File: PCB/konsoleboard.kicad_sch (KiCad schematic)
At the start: 0 parts

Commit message: Finished making the schematic, imma work on the PCB next
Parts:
- added A1: RaspberryPi_Pico, Module:RaspberryPi_Pico_Common_THT, symbol MCU_Module:RaspberryPi_Pico
- added BZ1: Buzzer, Buzzer_Beeper:Buzzer_Mallory_AST1109MLTRQ, symbol Device:Buzzer
- added SW1, SW10, SW2, SW3, SW4, SW5, SW6, SW7, SW8: SW_Push, Button_Switch_THT:SW_PUSH-12mm, symbol Switch:SW_Push
- added SW9: SW_Wuerth_450301014042, Button_Switch_THT:SW_Slide-03_Wuerth-WS-SLTV_10x2.5x6.4_P2.54mm, symbol Switch:SW_Wuerth_450301014042
- added U1: DM-OLED096-636, DM-OLED096-636:MODULE_DM-OLED096-636, symbol DM-OLED096-636:DM-OLED096-636
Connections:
- new net +3V3: A1.36 (3V3), SW9.1 (B), U1.2 (VCC_IN)
- new net BuzzerP: A1.16 (GPIO12), BZ1.1 (+)
- new net GND: A1.13 (GND), A1.18 (GND), A1.23 (GND), A1.28 (GND), A1.3 (GND), A1.38 (GND), A1.8 (GND), BZ1.2 (-), SW1.1, SW10.1, SW2.1, SW3.1, SW4.1, SW5.1, SW6.1, SW7.1, SW8.1, U1.1 (GND)
- new net LP1: A1.2 (GPIO1), SW1.2
- new net LP2: A1.4 (GPIO2), SW2.2
- new net LP3: A1.5 (GPIO3), SW3.2
- new net LP4: A1.6 (GPIO4), SW4.2
- new net RP1: A1.7 (GPIO5), SW5.2
- new net RP2: A1.9 (GPIO6), SW6.2
- new net RP3: A1.10 (GPIO7), SW7.2
- new net RP4: A1.11 (GPIO8), SW8.2
- new net RP5: A1.12 (GPIO9), SW10.2
- new net SCL: A1.15 (GPIO11), U1.3 (SCL)
- new net SDA: A1.14 (GPIO10), U1.4 (SDA)
- new net ToggleSwitch: A1.37 (3V3_EN), SW9.2 (C)
- no-connect marks 0 -> 20

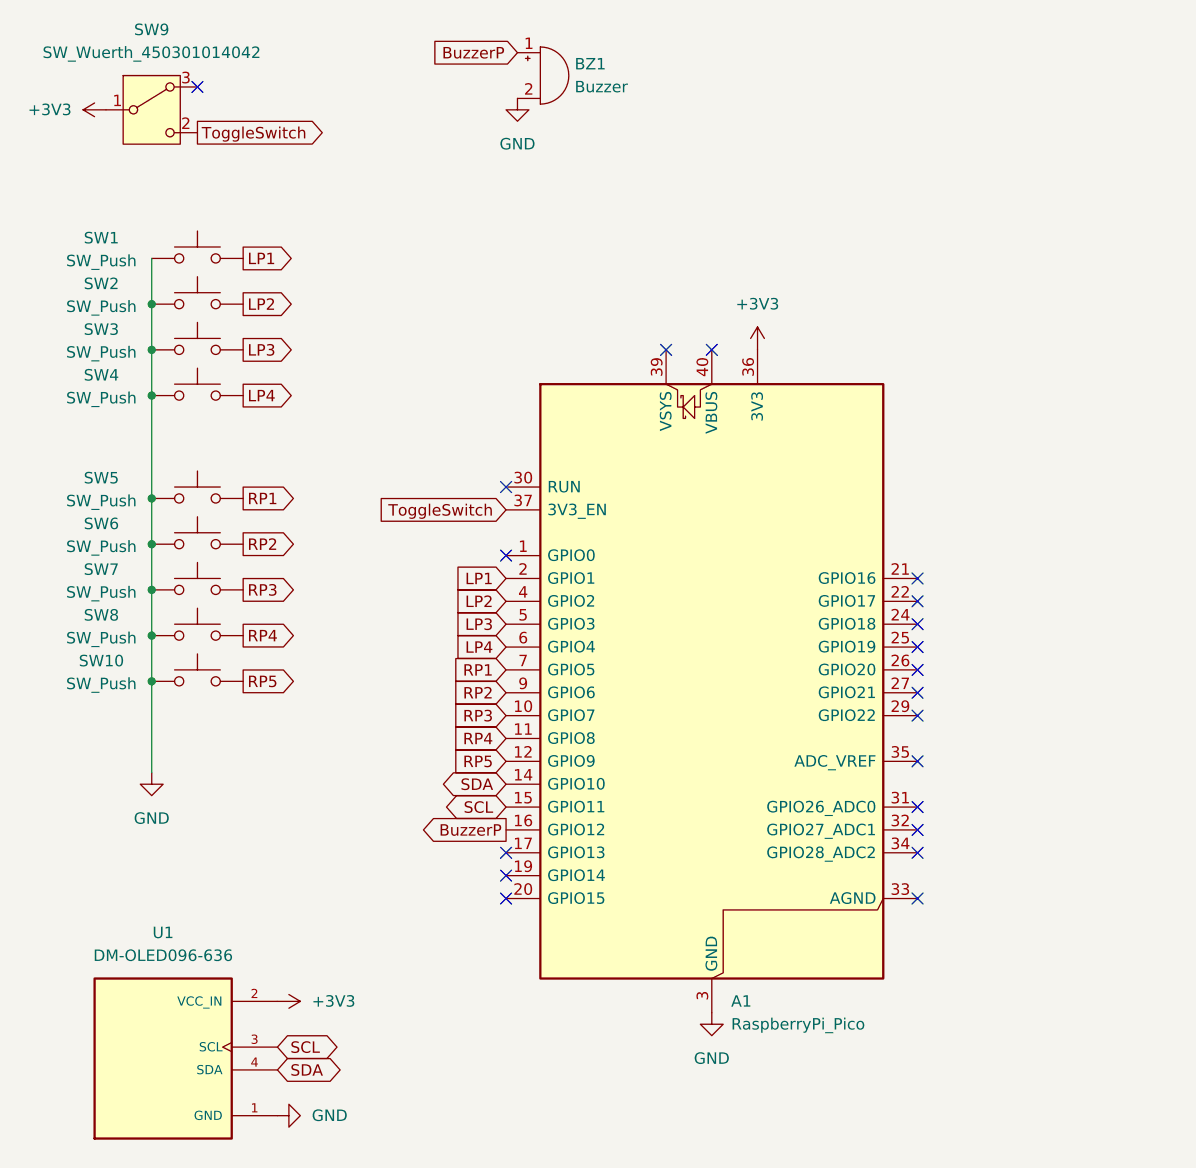
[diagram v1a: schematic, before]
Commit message: Added 2 more slide switch things for game pause and buzzer toggle, added a bigger display and repositioned most of the components
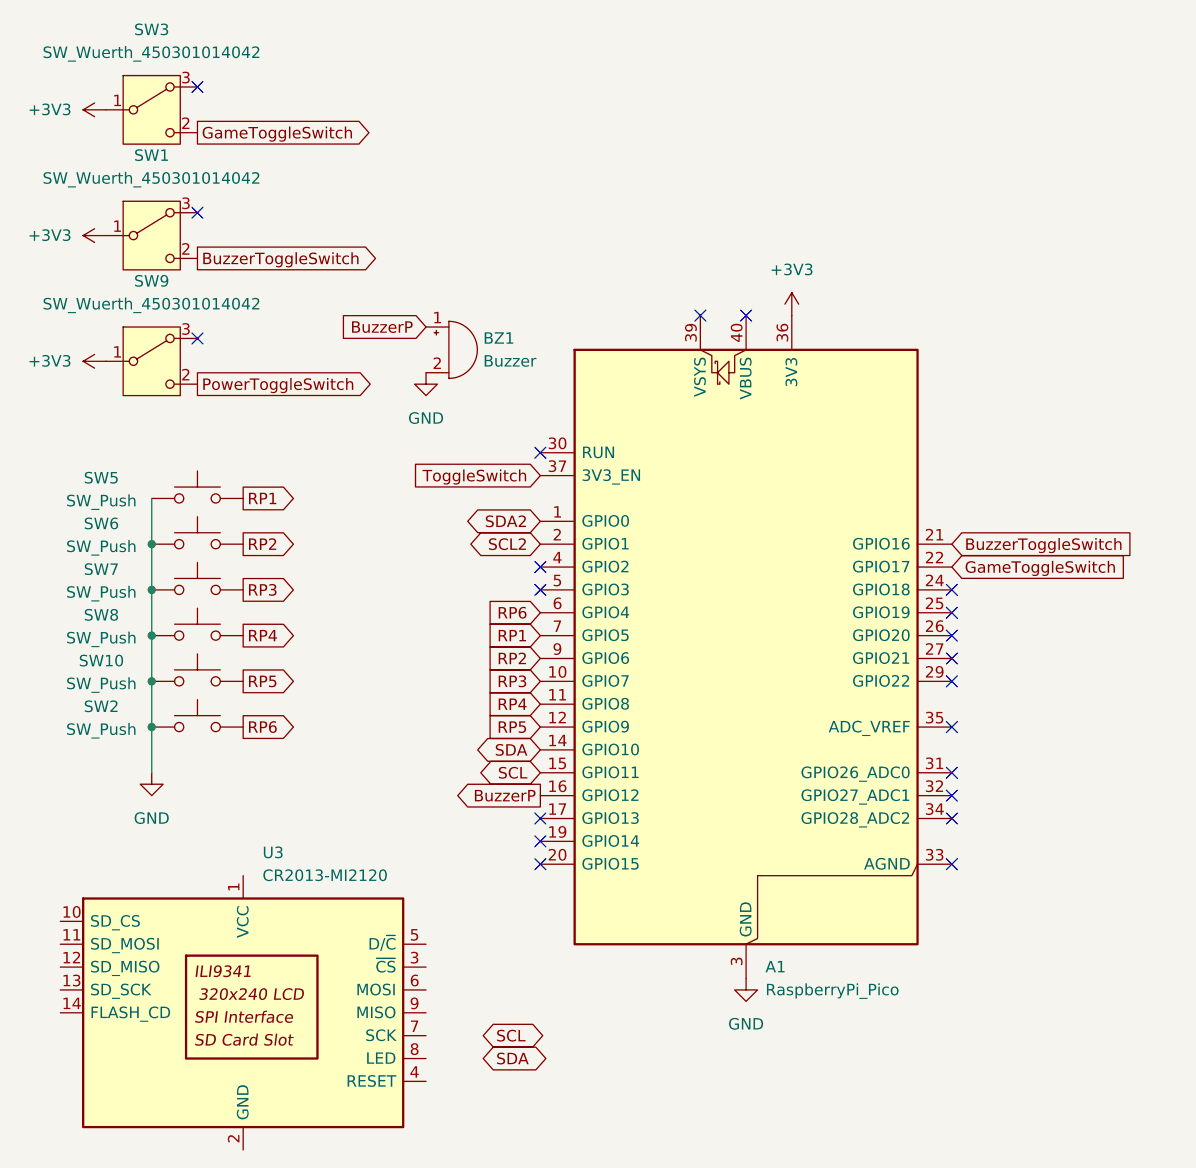
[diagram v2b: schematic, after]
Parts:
- removed SW1, SW3, SW4: SW_Push, Button_Switch_THT:SW_PUSH-12mm, symbol Switch:SW_Push
- removed U1: DM-OLED096-636, DM-OLED096-636:MODULE_DM-OLED096-636, symbol DM-OLED096-636:DM-OLED096-636
- added SW1, SW3: SW_Wuerth_450301014042, Button_Switch_THT:SW_Slide-03_Wuerth-WS-SLTV_10x2.5x6.4_P2.54mm, symbol Switch:SW_Wuerth_450301014042
- added U3: CR2013-MI2120, Display:CR2013-MI2120, symbol Driver_Display:CR2013-MI2120
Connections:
- net +3V3: now also SW1.1 (B), SW3.1 (B)
- net ToggleSwitch: no longer SW9.2 (C)
- net SDA2: now reaches A1.1 (GPIO0)
- net BuzzerToggleSwitch: now reaches A1.21 (GPIO16)
- net BuzzerToggleSwitch: now also SW1.2 (C)
- net GameToggleSwitch: now reaches A1.22 (GPIO17)
- net GameToggleSwitch: now also SW3.2 (C)
- net LP1 renamed SCL2
- net LP2: no longer names the net of A1.4 (GPIO2)
- net LP2: no longer SW2.2
- net LP3: no longer names the net of A1.5 (GPIO3)
- net LP4 renamed RP6
- net RP6: now also SW2.2
- new net PowerToggleSwitch: SW9.2 (C)
- no-connect marks 20 -> 21
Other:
- moved on the sheet: A1, BZ1, SW9

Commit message: Completed the pcb routing
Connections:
- net SCL is gone; now on net BuzzerToggleSwitch: A1.15 (GPIO11)
- net SCL2 is gone; now on net BuzzerP: A1.2 (GPIO1)
- net SDA is gone; now on net GameToggleSwitch: A1.14 (GPIO10)
- net SDA2 is gone; now on an unnamed net: A1.1 (GPIO0)
- net ToggleSwitch is gone; now on net PowerToggleSwitch: A1.37 (3V3_EN)
- net +3V3: now also U3.1 (VCC)
- net BuzzerP: no longer A1.16 (GPIO12)
- net BuzzerToggleSwitch: no longer A1.21 (GPIO16)
- net GameToggleSwitch: no longer A1.22 (GPIO17)
- net RP1: now also A1.11 (GPIO8); no longer A1.7 (GPIO5)
- net RP2: now also A1.10 (GPIO7); no longer A1.9 (GPIO6)
- net RP3: now also A1.9 (GPIO6); no longer A1.10 (GPIO7)
- net RP4: now also A1.7 (GPIO5); no longer A1.11 (GPIO8)
- net RP5: now also A1.6 (GPIO4); no longer A1.12 (GPIO9)
- net RP6: now also A1.5 (GPIO3); no longer A1.6 (GPIO4)
- net SD_CS: now reaches U3.10 (SD_CS)
- net SD_CS: now also A1.29 (GPIO22)
- net MOSI: now reaches U3.11 (SD_MOSI)
- net MOSI: now also A1.25 (GPIO19), U3.6 (MOSI)
- net MISO: now reaches U3.12 (SD_MISO)
- net MISO: now also A1.21 (GPIO16), U3.9 (MISO)
- net SCK: now reaches U3.13 (SD_SCK)
- net SCK: now also A1.24 (GPIO18), U3.7 (SCK)
- net FLASH_CD: now reaches U3.14 (FLASH_CD)
- net FLASH_CD: now also A1.27 (GPIO21)
- net at U3.3 (~{CS}): now also A1.12 (GPIO9)
- net at U3.4 (RESET): now also A1.16 (GPIO12)
- net at U3.8 (LED): now also A1.17 (GPIO13)
- no-connect marks 21 -> 13
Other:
- moved on the sheet: BZ1, SW1, SW10, SW2, SW3, SW5, SW6, SW7, SW8, SW9

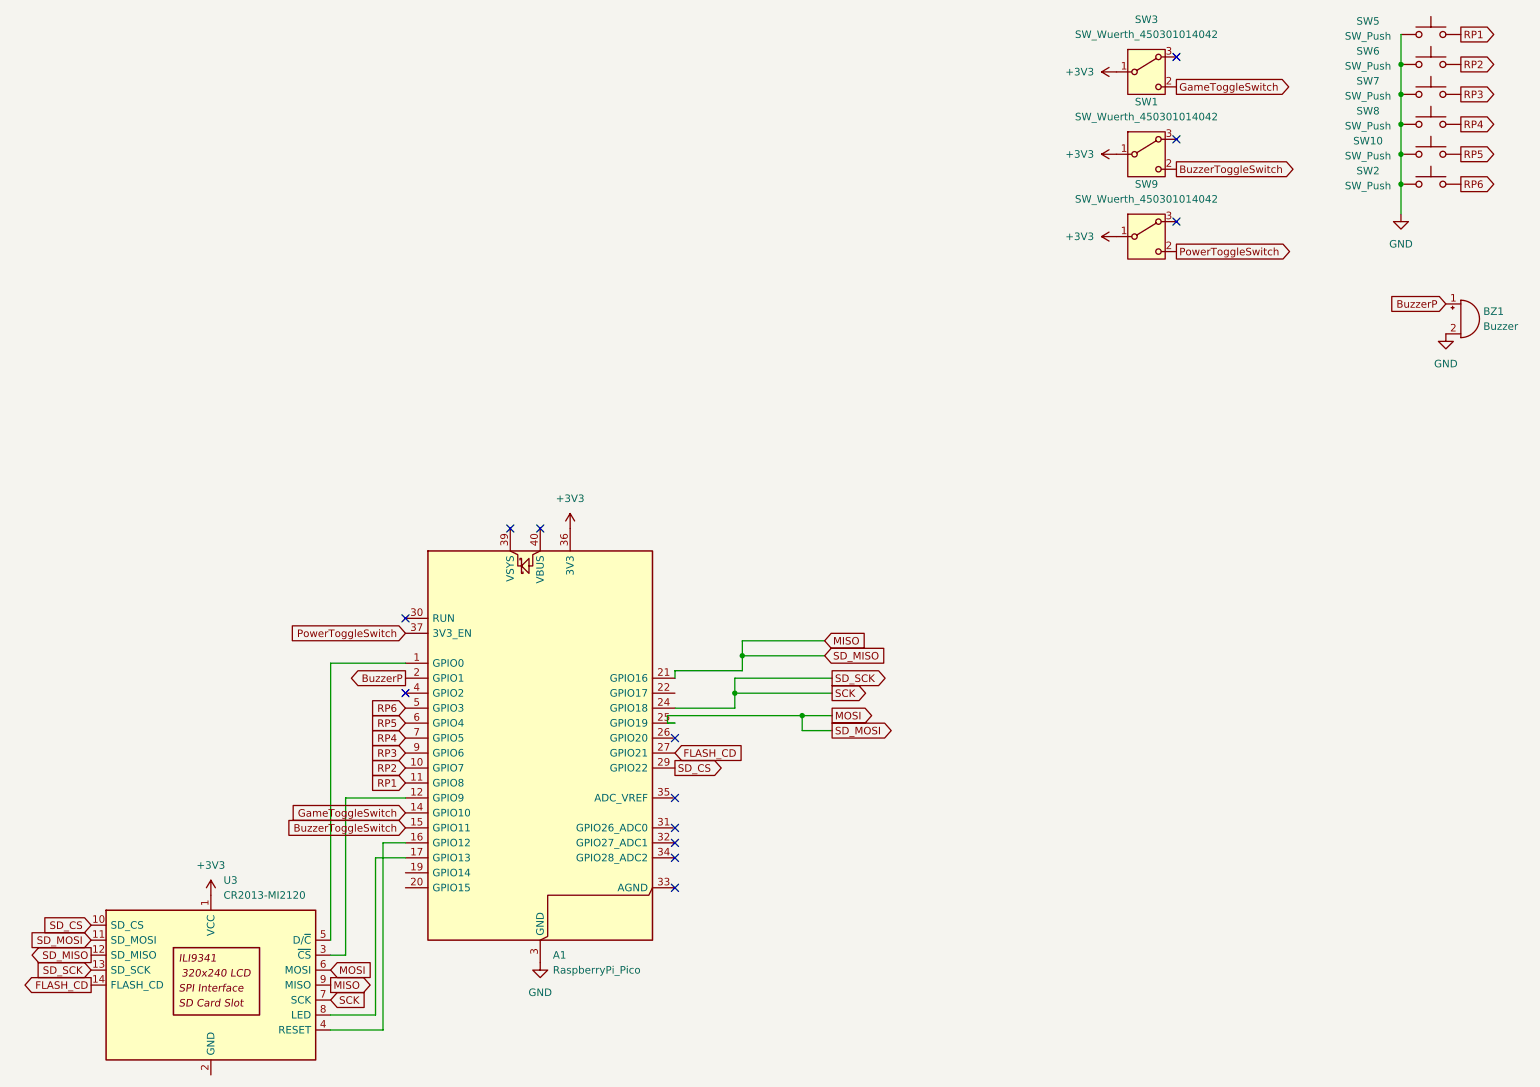
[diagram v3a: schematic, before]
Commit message: Decided to remove the buzzer and the buzzer switch
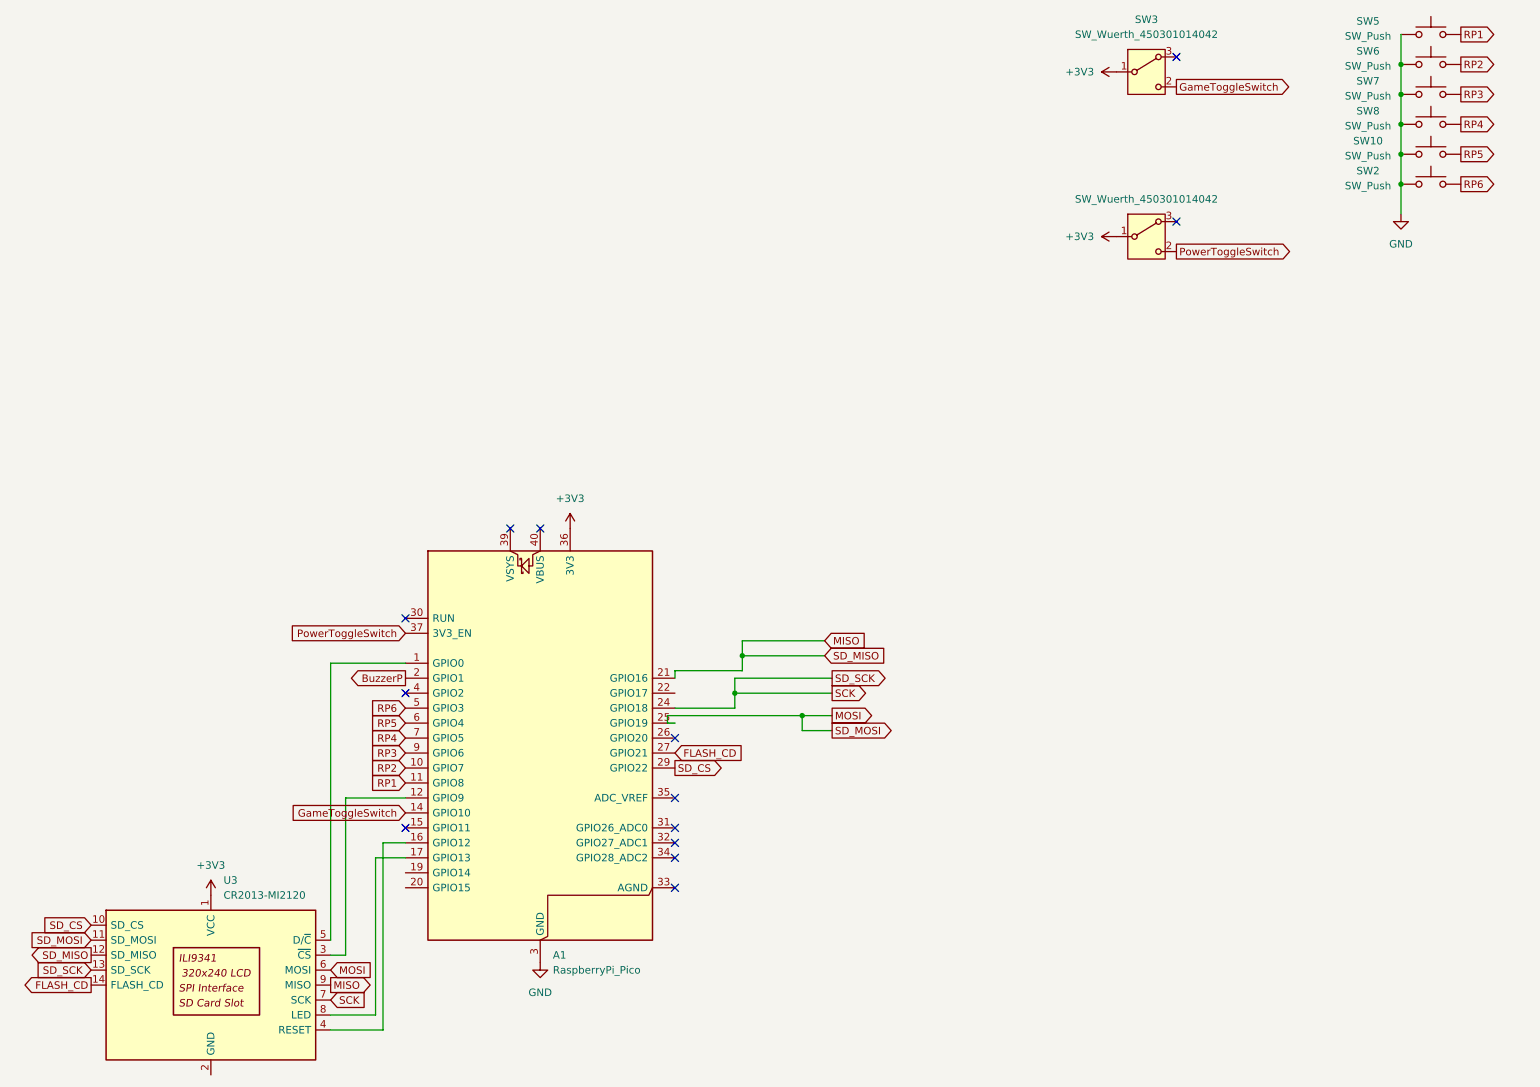
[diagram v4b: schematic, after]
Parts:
- removed BZ1: Buzzer, Buzzer_Beeper:Buzzer_Mallory_AST1109MLTRQ, symbol Device:Buzzer
- removed SW1: SW_Wuerth_450301014042, Button_Switch_THT:SW_Slide-03_Wuerth-WS-SLTV_10x2.5x6.4_P2.54mm, symbol Switch:SW_Wuerth_450301014042
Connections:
- net BuzzerToggleSwitch: no longer names the net of A1.15 (GPIO11)
